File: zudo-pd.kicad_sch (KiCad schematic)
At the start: 0 parts

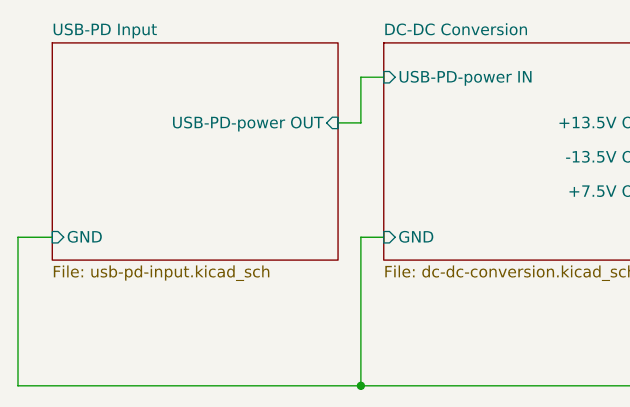
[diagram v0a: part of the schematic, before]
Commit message: Update KiCad schematics for STUSB4500 v1.1 design
- Update USB-PD input stage with STUSB4500 + Q1 load switch
- Simplify output stage to single 16-pin connector (J2)
- Update FASTON terminal designators (J6-J9)

Co-Authored-By: Claude Opus 4.5 <noreply@anthropic.com>
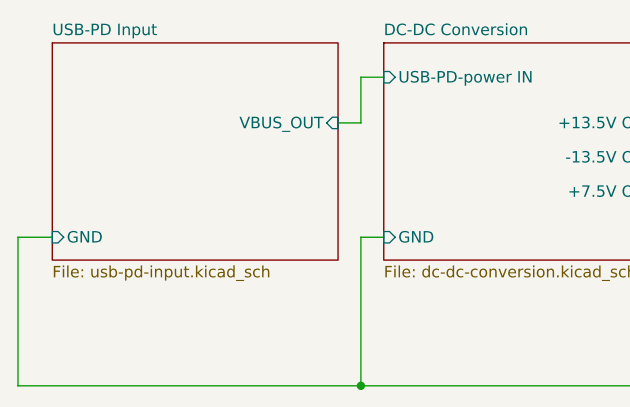
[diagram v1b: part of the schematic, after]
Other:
- sheet USB-PD Input ports: added VBUS_OUT; removed USB-PD-power OUT
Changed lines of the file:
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@@
 			)
 		)
-		(pin "USB-PD-power OUT" input
+		(pin "VBUS_OUT" input
 			(at 64.77 35.56 0)
 			(effects
